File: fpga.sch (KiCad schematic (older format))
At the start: 23 parts, among them IC1 EP4CE10F17, J1 Pinheader_2x5_TH_WALL

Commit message: Update
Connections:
- net labels added: CMD, CS#, ETH_SD[0:15], INT, IOR#, IORST#, IOW#
- wire segments 139 -> 145

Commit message: Sch/pcb update
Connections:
- net labels added: ETH_SD0, ETH_SD1, ETH_SD10, ETH_SD11, ETH_SD12, ETH_SD13, ETH_SD14, ETH_SD15, ETH_SD2, ETH_SD3, ETH_SD4, ETH_SD5, ETH_SD6, ETH_SD7, ETH_SD8, ETH_SD9
- wire segments 145 -> 161
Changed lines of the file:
@@
 Text HLabel 2225 4975 0    60   Input ~ 0
 nSLAVEn_IN
-Text HLabel 14950 7800 2    60   Output ~ 0
+Text HLabel 15225 6150 2    60   Output ~ 0
 CMD
-Text HLabel 14950 7875 2    60   Input ~ 0
+Text HLabel 15225 6225 2    60   Input ~ 0
 INT
-Text HLabel 14950 7950 2    60   Output ~ 0
+Text HLabel 15225 6300 2    60   Output ~ 0
 IOR#
-Text HLabel 14950 8025 2    60   Output ~ 0
+Text HLabel 15225 6375 2    60   Output ~ 0
 IOW#
-Text HLabel 14950 8100 2    60   Output ~ 0
+Text HLabel 15225 6450 2    60   Output ~ 0
 CS#
-Text HLabel 14950 8175 2    60   Output ~ 0
+Text HLabel 15225 6525 2    60   Output ~ 0
 IORST#
-Text HLabel 14975 6675 2    60   BiDi ~ 0
+Text HLabel 15200 6725 2    60   BiDi ~ 0
 ETH_SD[0:15]
 Wire Wire Line
@@
 Connection ~ 12550 2725
 Wire Wire Line
-	14950 7800 14325 7800
-Wire Wire Line
-	14950 7875 14325 7875
-Wire Wire Line
-	14950 7950 14325 7950
-Wire Wire Line
-	14950 8025 14325 8025
-Wire Wire Line
-	14950 8100 14325 8100
-Wire Wire Line
-	14950 8175 14325 8175
-Text Label 14375 7800 0    50   ~ 0
+	15225 6150 14400 6150
+Wire Wire Line
+	15225 6225 14400 6225
+Wire Wire Line
+	15225 6300 14400 6300
+Wire Wire Line
+	15225 6375 14400 6375
+Wire Wire Line
+	15225 6450 14400 6450
+Wire Wire Line
+	15225 6525 14400 6525
+Text Label 14450 6150 0    50   ~ 0
 CMD
-Text Label 14375 7875 0    50   ~ 0
+Text Label 14450 6225 0    50   ~ 0
 INT
-Text Label 14375 7950 0    50   ~ 0
+Text Label 14450 6300 0    50   ~ 0
 IOR#
+Text Label 14450 6375 0    50   ~ 0
+IOW#
+Text Label 14450 6450 0    50   ~ 0
+CS#
+Text Label 14450 6525 0    50   ~ 0
+IORST#
+Wire Bus Line
+	15200 6725 15100 6725
+Wire Bus Line
+	15100 6725 15100 8425
+Wire Wire Line
+	15000 6825 14375 6825
+Entry Wire Line
+	15000 6825 15100 6925
+Entry Wire Line
+	15000 6925 15100 7025
+Entry Wire Line
+	15000 7025 15100 7125
+Entry Wire Line
+	15000 7125 15100 7225
+Entry Wire Line
+	15000 7225 15100 7325
+Entry Wire Line
+	15000 7325 15100 7425
+Entry Wire Line
+	15000 7425 15100 7525
+Entry Wire Line
+	15000 7525 15100 7625
+Entry Wire Line
+	15000 7625 15100 7725
+Entry Wire Line
+	15000 7725 15100 7825
+Entry Wire Line
+	15000 7825 15100 7925
+Entry Wire Line
+	15000 7925 15100 8025
+Entry Wire Line
+	15000 8025 15100 8125
+Entry Wire Line
+	15000 8125 15100 8225
+Entry Wire Line
+	15000 8225 15100 8325
+Entry Wire Line
+	15000 8325 15100 8425
+Wire Wire Line
+	15000 6925 14375 6925
+Wire Wire Line
+	15000 7025 14375 7025
+Wire Wire Line
+	15000 7125 14375 7125
+Wire Wire Line
+	15000 7225 14375 7225
+Wire Wire Line
+	15000 7325 14375 7325
+Wire Wire Line
+	15000 7425 14375 7425
+Wire Wire Line
+	15000 7525 14375 7525
+Wire Wire Line
+	15000 7625 14375 7625
+Wire Wire Line
+	15000 7725 14375 7725
+Wire Wire Line
+	15000 7825 14375 7825
+Wire Wire Line
+	15000 7925 14375 7925
+Wire Wire Line
+	15000 8025 14375 8025
+Wire Wire Line
+	15000 8125 14375 8125
+Wire Wire Line
+	15000 8225 14375 8225
+Wire Wire Line
+	15000 8325 14375 8325
+Text Label 14375 6825 0    50   ~ 0
+ETH_SD0
+Text Label 14375 6925 0    50   ~ 0
+ETH_SD1
+Text Label 14375 7025 0    50   ~ 0
+ETH_SD2
+Text Label 14375 7125 0    50   ~ 0
+ETH_SD3
+Text Label 14375 7225 0    50   ~ 0
+ETH_SD4
+Text Label 14375 7325 0    50   ~ 0
+ETH_SD5
+Text Label 14375 7425 0    50   ~ 0
+ETH_SD6
+Text Label 14375 7525 0    50   ~ 0
+ETH_SD7
+Text Label 14375 7625 0    50   ~ 0
+ETH_SD8
+Text Label 14375 7725 0    50   ~ 0
+ETH_SD9
+Text Label 14375 7825 0    50   ~ 0
+ETH_SD10
+Text Label 14375 7925 0    50   ~ 0
+ETH_SD11
 Text Label 14375 8025 0    50   ~ 0
-IOW#
-Text Label 14375 8100 0    50   ~ 0
-CS#
-Text Label 14375 8175 0    50   ~ 0
-IORST#
+ETH_SD12
+Text Label 14375 8125 0    50   ~ 0
+ETH_SD13
+Text Label 14375 8225 0    50   ~ 0
+ETH_SD14
+Text Label 14375 8325 0    50   ~ 0
+ETH_SD15
 $EndSCHEMATC

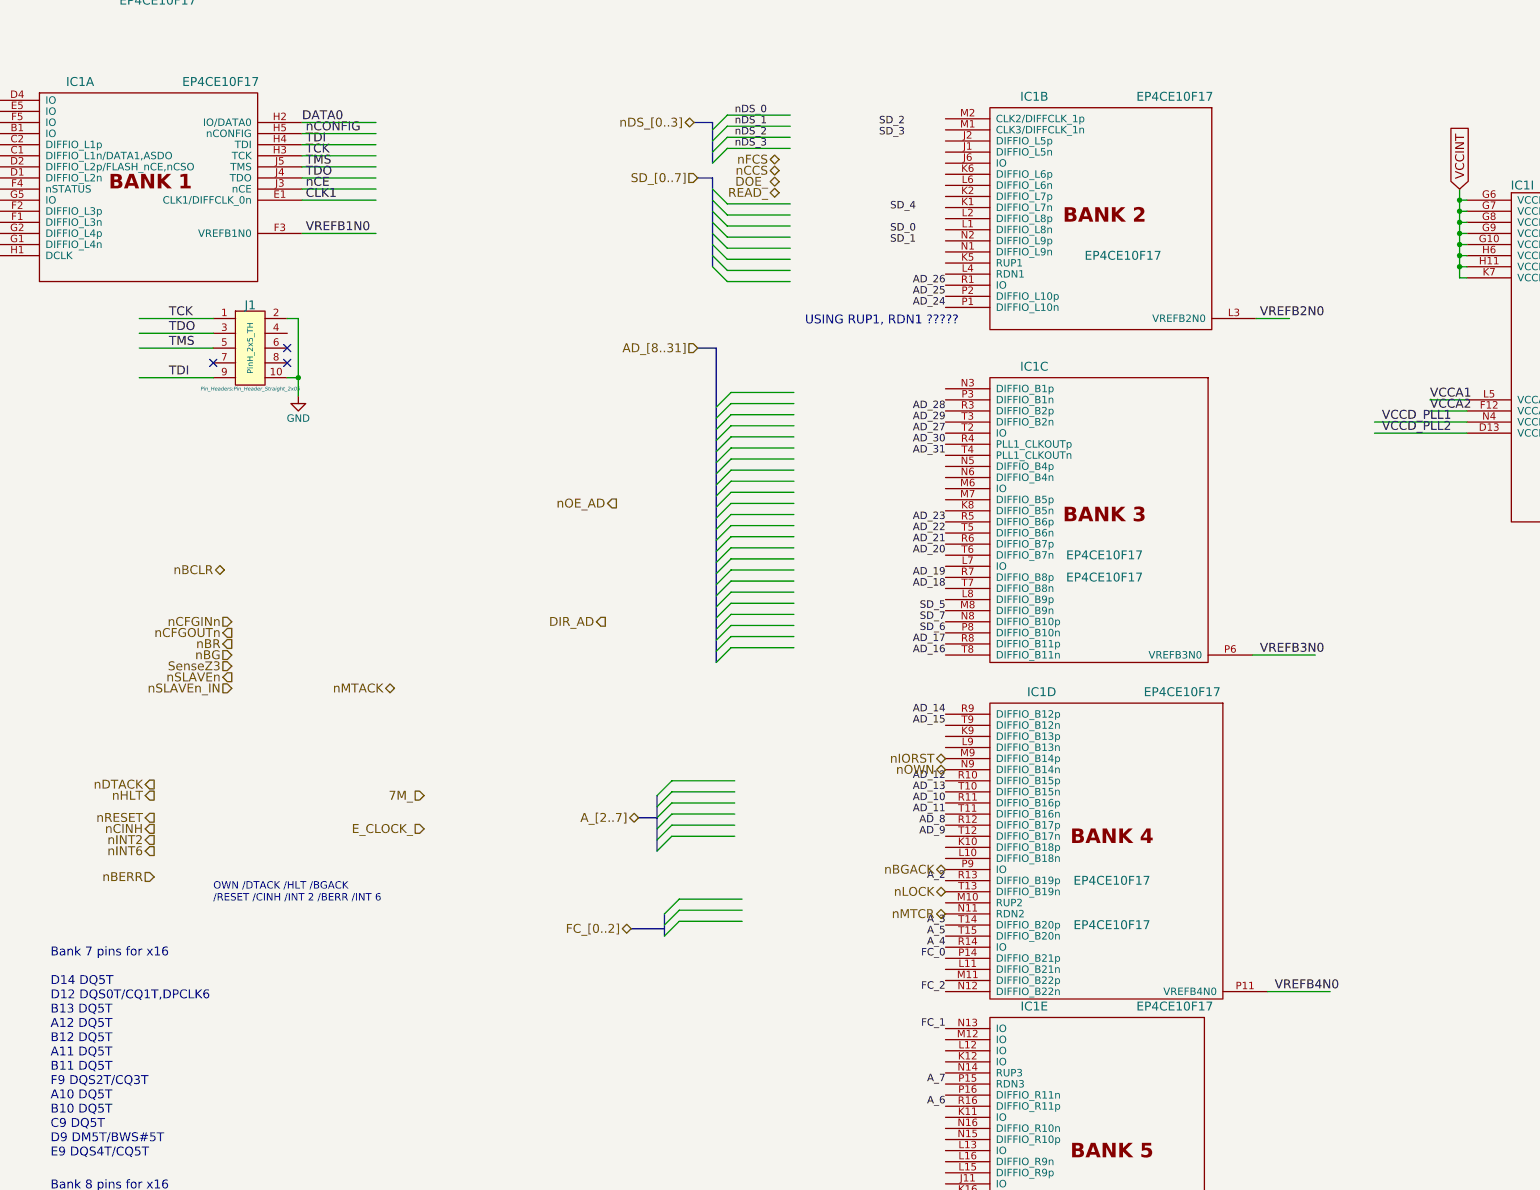
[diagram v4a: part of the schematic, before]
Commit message: Swapping signals
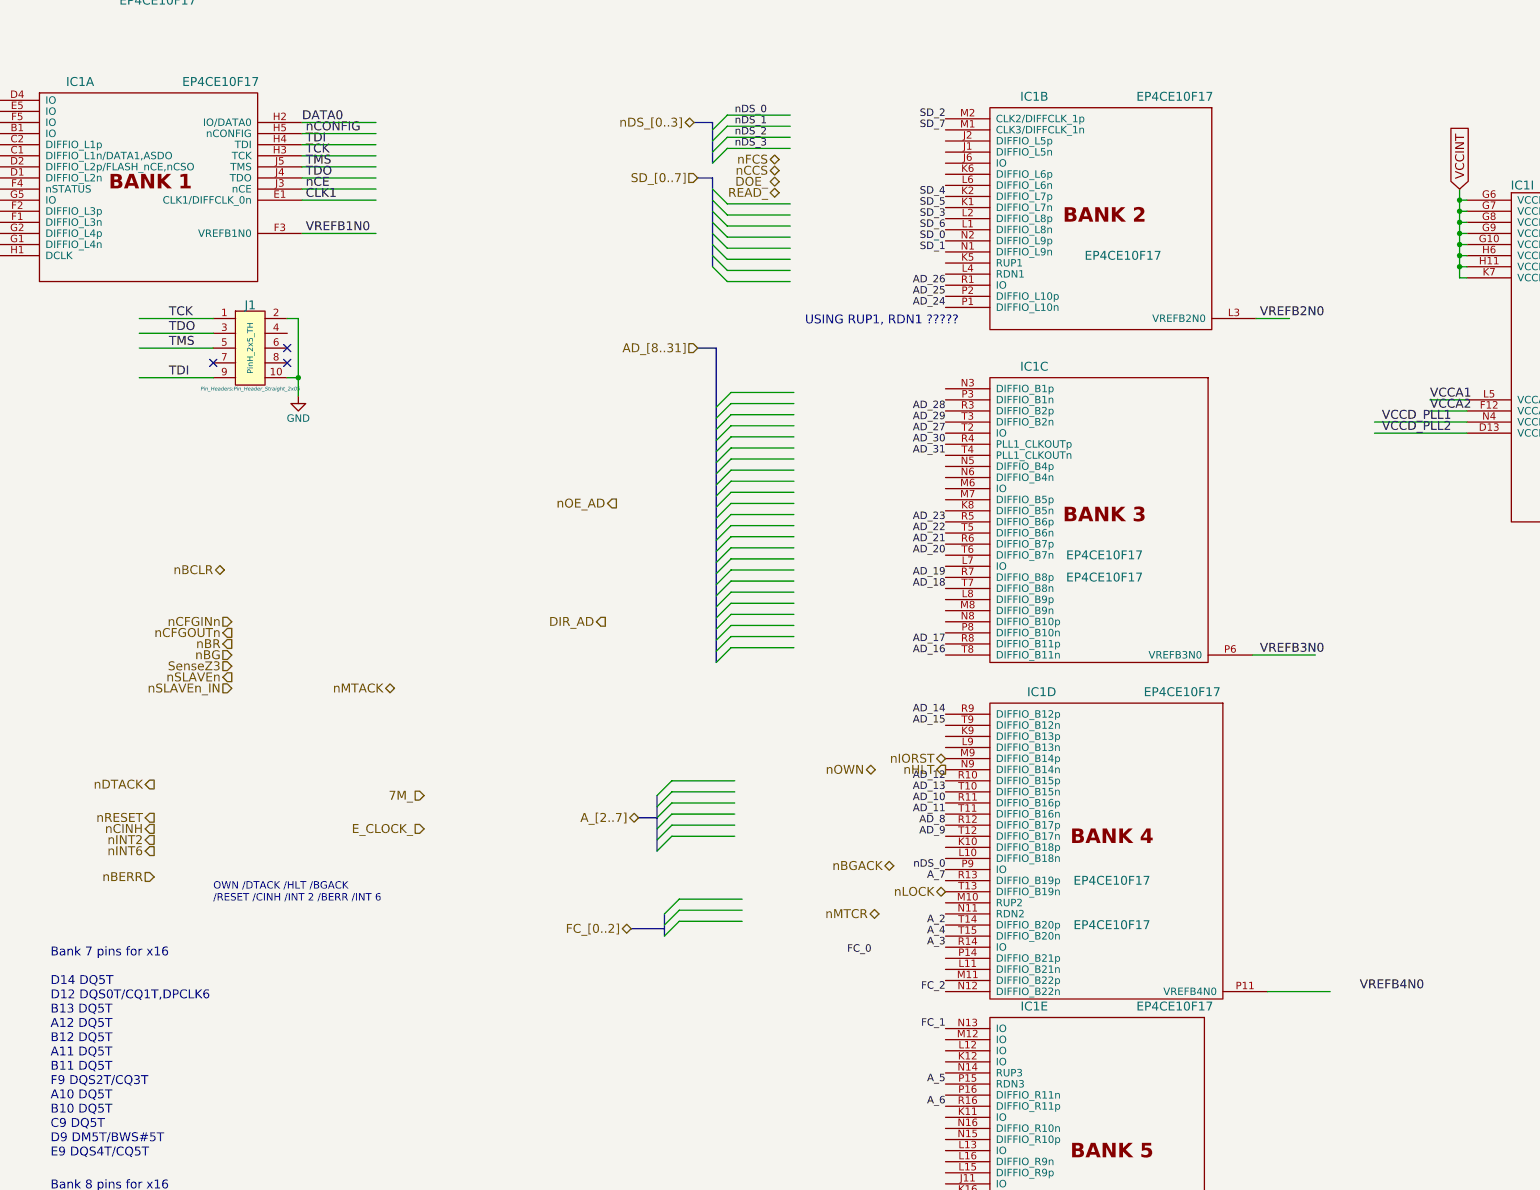
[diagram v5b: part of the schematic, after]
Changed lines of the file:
@@
 $EndComp
 $Comp
-L GND #PWR2
+L GND #PWR01
 U 1 1 5807C448
 P 12075 6725
-F 0 "#PWR2" H 12075 6475 50  0001 C CNN
+F 0 "#PWR01" H 12075 6475 50  0001 C CNN
 F 1 "GND" H 12075 6575 50  0000 C CNN
 F 2 "" H 12075 6725 50  0000 C CNN
@@
 Entry Wire Line
 	5475 2125 5575 2225
-Text Label 6850 1900 2    50   ~ 0
+Text Label 7050 1950 2    50   ~ 0
 SD_0
-Text Label 6850 1975 2    50   ~ 0
+Text Label 7050 2025 2    50   ~ 0
 SD_1
-Text Label 6775 1175 2    50   ~ 0
+Text Label 7050 1125 2    50   ~ 0
 SD_2
-Text Label 6775 1250 2    50   ~ 0
+Text Label 7050 1800 2    50   ~ 0
 SD_3
-Text Label 6850 1750 2    50   ~ 0
+Text Label 7050 1650 2    50   ~ 0
 SD_4
-Text Label 7050 4450 2    50   ~ 0
+Text Label 7050 1725 2    50   ~ 0
 SD_5
-Text Label 7050 4600 2    50   ~ 0
+Text Label 7050 1875 2    50   ~ 0
 SD_6
-Text Label 7050 4525 2    50   ~ 0
+Text Label 7050 1200 2    50   ~ 0
 SD_7
 Entry Wire Line
@@
 Entry Wire Line
 	5150 6650 5250 6550
-Text Label 7050 6800 2    50   ~ 0
+Text Label 6550 6775 2    50   ~ 0
 FC_0
 $Comp
@@
 Text HLabel 3325 4975 0    60   BiDi ~ 0
 nMTACK
-Text HLabel 7050 6500 0    60   BiDi ~ 0
+Text HLabel 6600 6500 0    60   BiDi ~ 0
 nMTCR
 Text HLabel 4975 5850 0    60   BiDi ~ 0
@@
 Entry Wire Line
 	5100 5700 5200 5600
-Text Label 7050 6275 2    50   ~ 0
+Text Label 7050 6575 2    50   ~ 0
 A_2
 Entry Wire Line
@@
 Entry Wire Line
 	5100 6075 5200 5975
-Text Label 7050 6575 2    50   ~ 0
+Text Label 7050 6725 2    50   ~ 0
 A_3
-Text Label 7050 6650 2    50   ~ 0
+Text Label 7050 7650 2    50   ~ 0
 A_5
 Text Label 7050 7800 2    50   ~ 0
 A_6
-Text Label 7050 7650 2    50   ~ 0
-A_7
 Text HLabel 2225 4525 0    60   Input ~ 0
 nCFGINn
@@
 Text HLabel 1700 5625 0    60   Output ~ 0
 nDTACK
-Text HLabel 1700 5700 0    60   Output ~ 0
+Text HLabel 7050 5525 0    60   Output ~ 0
 nHLT
 Text Notes 2100 6425 0    50   ~ 0
@@
 $EndComp
 $Comp
-L GND #PWR1
+L GND #PWR02
 U 1 1 57F7A288
 P 2675 3000
-F 0 "#PWR1" H 2675 2750 50  0001 C CNN
+F 0 "#PWR02" H 2675 2750 50  0001 C CNN
 F 1 "GND" H 2675 2850 50  0000 C CNN
 F 2 "" H 2675 3000 50  0000 C CNN
@@
 NoConn ~ 2600 2775
 $Comp
-L +3V3 #PWR4
+L +3V3 #PWR03
 U 1 1 57F8D5C6
 P 13775 2025
-F 0 "#PWR4" H 13875 2075 20  0001 C CNN
+F 0 "#PWR03" H 13875 2075 20  0001 C CNN
 F 1 "+3V3" H 13775 2115 30  0000 C CNN
 F 2 "" H 13775 2025 60  0000 C CNN
@@
 	1    0    0    -1
 $EndComp
-Text Label 9275 7025 0    60   ~ 0
+Text Label 9850 7025 0    60   ~ 0
 VREFB4N0
 Text Label 9175 4750 0    60   ~ 0
@@
 $EndComp
 $Comp
-L GND #PWR5
+L GND #PWR04
 U 1 1 57F8FD8F
 P 13775 2325
-F 0 "#PWR5" H 13775 2075 50  0001 C CNN
+F 0 "#PWR04" H 13775 2075 50  0001 C CNN
 F 1 "GND" H 13775 2175 50  0000 C CNN
 F 2 "" H 13775 2325 50  0000 C CNN
@@
 $EndComp
 $Comp
-L GND #PWR3
+L GND #PWR05
 U 1 1 57F90743
 P 13275 1400
-F 0 "#PWR3" H 13275 1150 50  0001 C CNN
+F 0 "#PWR05" H 13275 1150 50  0001 C CNN
 F 1 "GND" H 13275 1250 50  0000 C CNN
 F 2 "" H 13275 1400 50  0000 C CNN
@@
 	1    0    0    -1
 $EndComp
-Text HLabel 7050 6200 0    60   BiDi ~ 0
+Text HLabel 6700 6175 0    60   BiDi ~ 0
 nBGACK
-Text HLabel 7050 5525 0    60   BiDi ~ 0
+Text HLabel 6575 5525 0    60   BiDi ~ 0
 nOWN
 Text HLabel 3525 5700 0    60   Input ~ 0
@@
 	1    0    0    -1
 $EndComp
-Text Label 7050 6725 2    50   ~ 0
+Text Label 7050 6650 2    50   ~ 0
 A_4
 $Comp
@@
 Text Label 14375 8325 0    50   ~ 0
 ETH_SD15
+Text Label 7050 6275 2    50   ~ 0
+A_7
+Text Label 7050 6200 2    50   ~ 0
+nDS_0
 $EndSCHEMATC

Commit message: Swapping, bottom side
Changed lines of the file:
@@
 Entry Wire Line
 	5150 6575 5250 6475
+Text Label 7050 6500 2    50   ~ 0
+FC_2
+Text Label 9650 7025 0    50   ~ 0
+FC_1
+Entry Wire Line
+	5150 6650 5250 6550
 Text Label 7050 7025 2    50   ~ 0
-FC_2
-Text Label 7050 7275 2    50   ~ 0
-FC_1
-Entry Wire Line
-	5150 6650 5250 6550
-Text Label 6550 6775 2    50   ~ 0
 FC_0
 $Comp
@@
 Text HLabel 3325 4975 0    60   BiDi ~ 0
 nMTACK
-Text HLabel 6600 6500 0    60   BiDi ~ 0
+Text HLabel 7050 7275 0    60   BiDi ~ 0
 nMTCR
 Text HLabel 4975 5850 0    60   BiDi ~ 0
@@
 	1    0    0    -1
 $EndComp
-Text Label 9850 7025 0    60   ~ 0
+Text Label 10050 6775 0    60   ~ 0
 VREFB4N0
 Text Label 9175 4750 0    60   ~ 0
@@
 Text HLabel 6700 6175 0    60   BiDi ~ 0
 nBGACK
-Text HLabel 6575 5525 0    60   BiDi ~ 0
+Text HLabel 7050 6800 0    60   BiDi ~ 0
 nOWN
 Text HLabel 3525 5700 0    60   Input ~ 0
